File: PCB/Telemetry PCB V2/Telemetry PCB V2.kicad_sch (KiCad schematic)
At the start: 47 parts, among them IC1 E22-900M22S, J1 USB_C_Receptacle_USB2.0_16P, J2 Batt, J3 Serial Debug Header 1x4, J4 GPS, J5 Conn_01x04_Pin, SW1 SW_MEC_5E, SW2 SW_MEC_5E, U1 AP62200WU, U2 STM32F411CEUx, U3 MCP1700x-250xxTT, Y1 25MHZ 20pF, Y2 32.768k 12.5pF

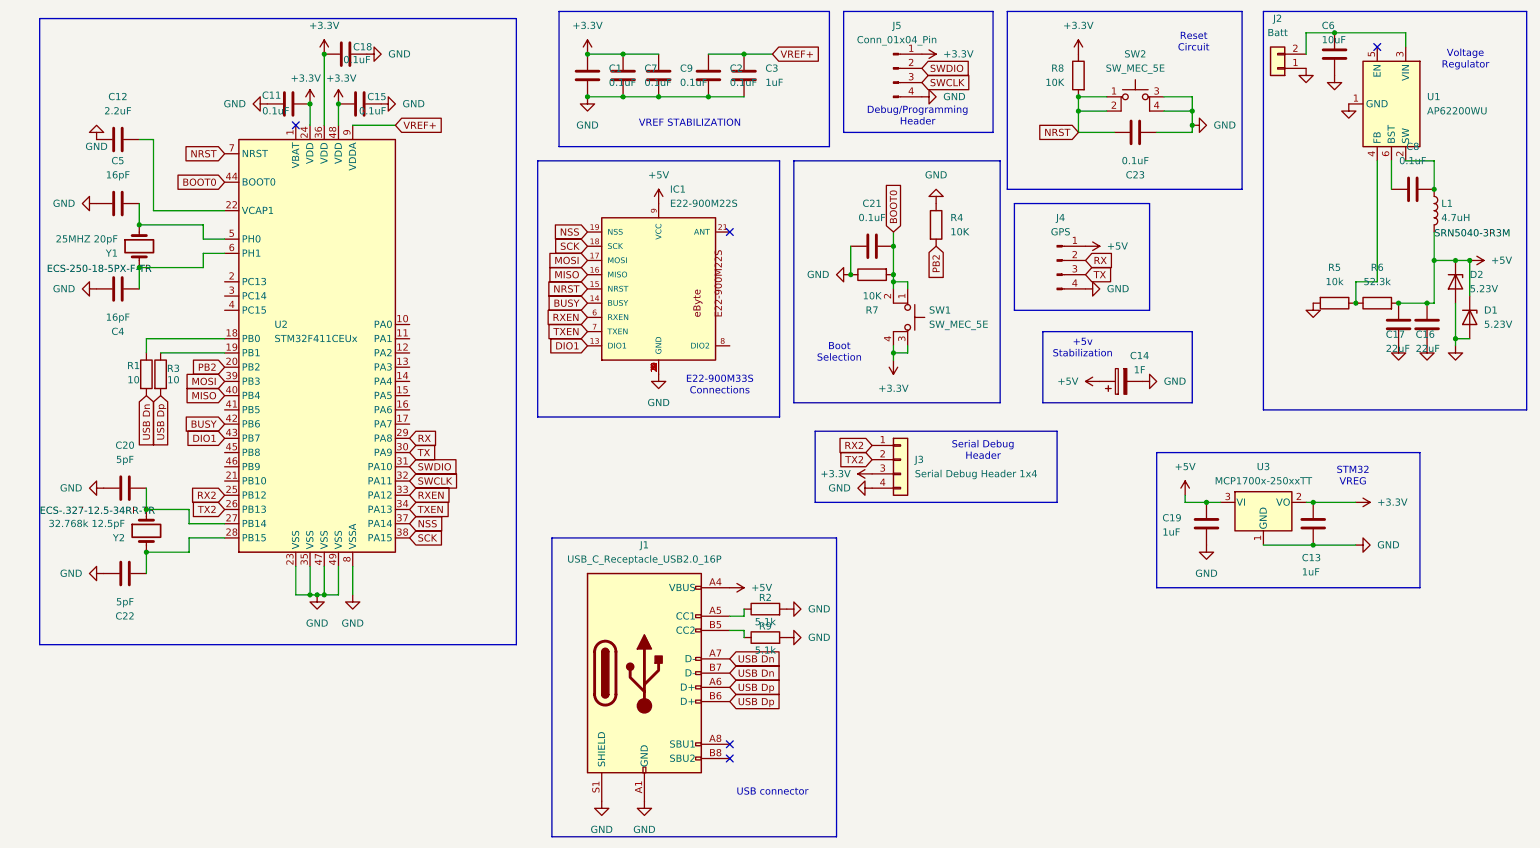
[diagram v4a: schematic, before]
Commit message: Corrected spi and uart connections
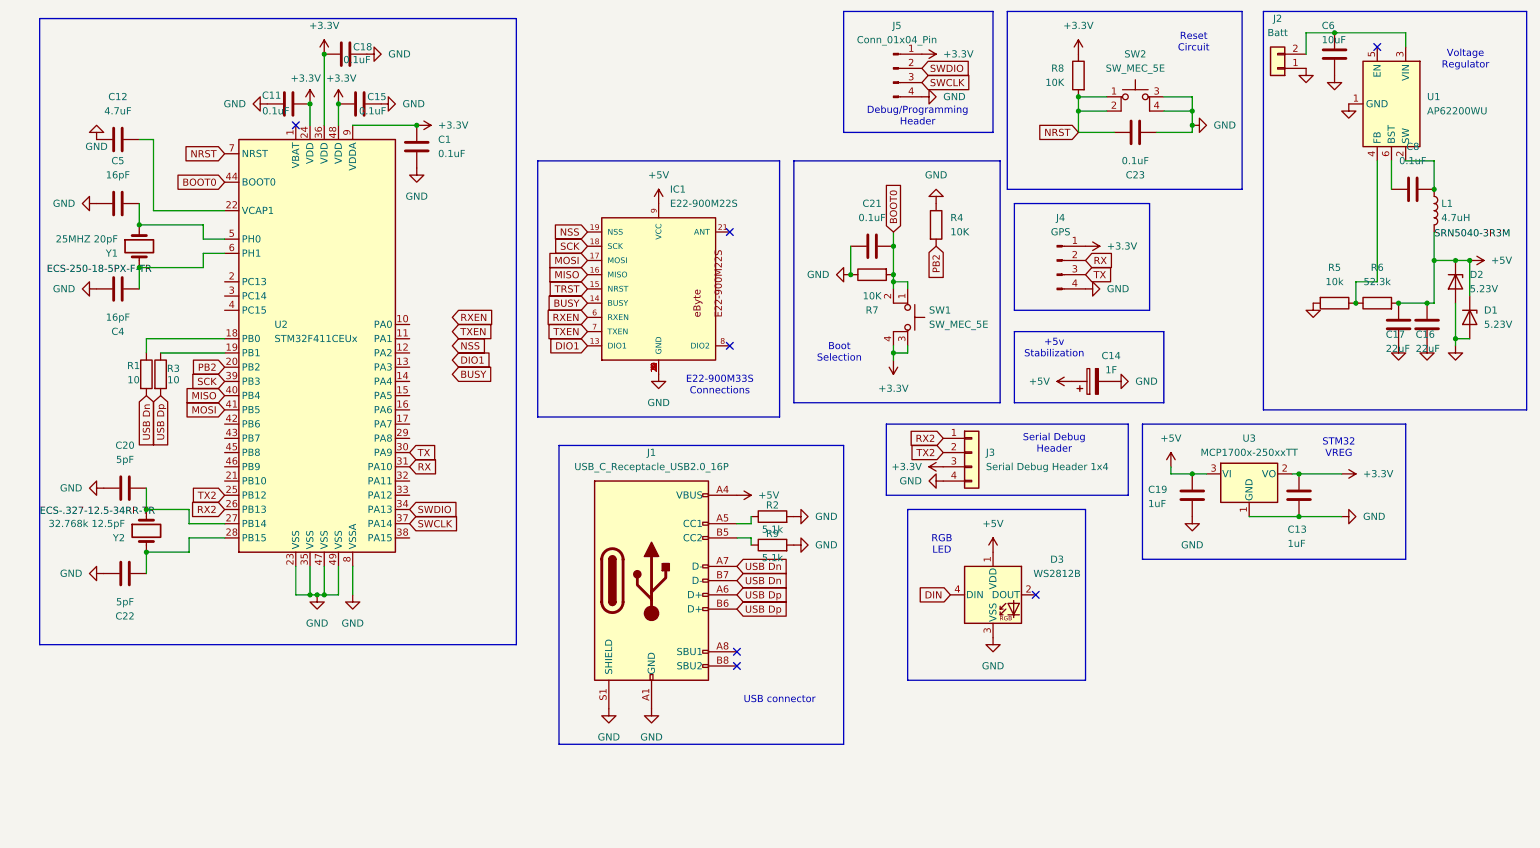
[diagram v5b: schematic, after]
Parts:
- removed C2, C7, C9: 0.1uF, Capacitor_SMD:C_1206_3216Metric_Pad1.33x1.80mm_HandSolder, symbol Device:C
- removed C3: 1uF, Capacitor_SMD:C_1206_3216Metric_Pad1.33x1.80mm_HandSolder, symbol Device:C
- added D3: WS2812B, LED_SMD:LED_WS2812B_PLCC4_5.0x5.0mm_P3.2mm, symbol LED:WS2812B
- C12: value 2.2uF -> 4.7uF
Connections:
- net VREF+ is gone; now on net +3.3V: U2.9 (VDDA)
- net +3.3V: now also C1.2, J4.1 (Pin_1); no longer C1.1
- net +5V: now also D3.1 (VDD); no longer J4.1 (Pin_1)
- net BUSY: no longer U2.42 (PB6)
- net DIO1: no longer U2.43 (PB7)
- net GND: now also C1.1, D3.3 (VSS); no longer C1.2
- net MOSI: now also U2.41 (PB5); no longer U2.39 (PB3)
- net NRST: no longer IC1.15 (NRST)
- net NSS: no longer U2.37 (PA14)
- net RX: now also U2.31 (PA10); no longer U2.29 (PA8)
- net RX2: now also U2.26 (PB13); no longer U2.25 (PB12)
- net RXEN: no longer U2.33 (PA12)
- net SCK: now also U2.39 (PB3); no longer U2.38 (PA15)
- net SWCLK: now also U2.37 (PA14); no longer U2.32 (PA11)
- net SWDIO: now also U2.34 (PA13); no longer U2.31 (PA10)
- net TX2: now also U2.25 (PB12); no longer U2.26 (PB13)
- net TXEN: no longer U2.34 (PA13)
- new net DIN: D3.4 (DIN)
- new net TRST: IC1.15 (NRST)
- no-connect marks 5 -> 7
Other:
- note added: "RGB LED"
- note removed: "VREF STABILIZATION"
- moved on the sheet: C13, C14, C19, J1, J3, R2, R9, U3

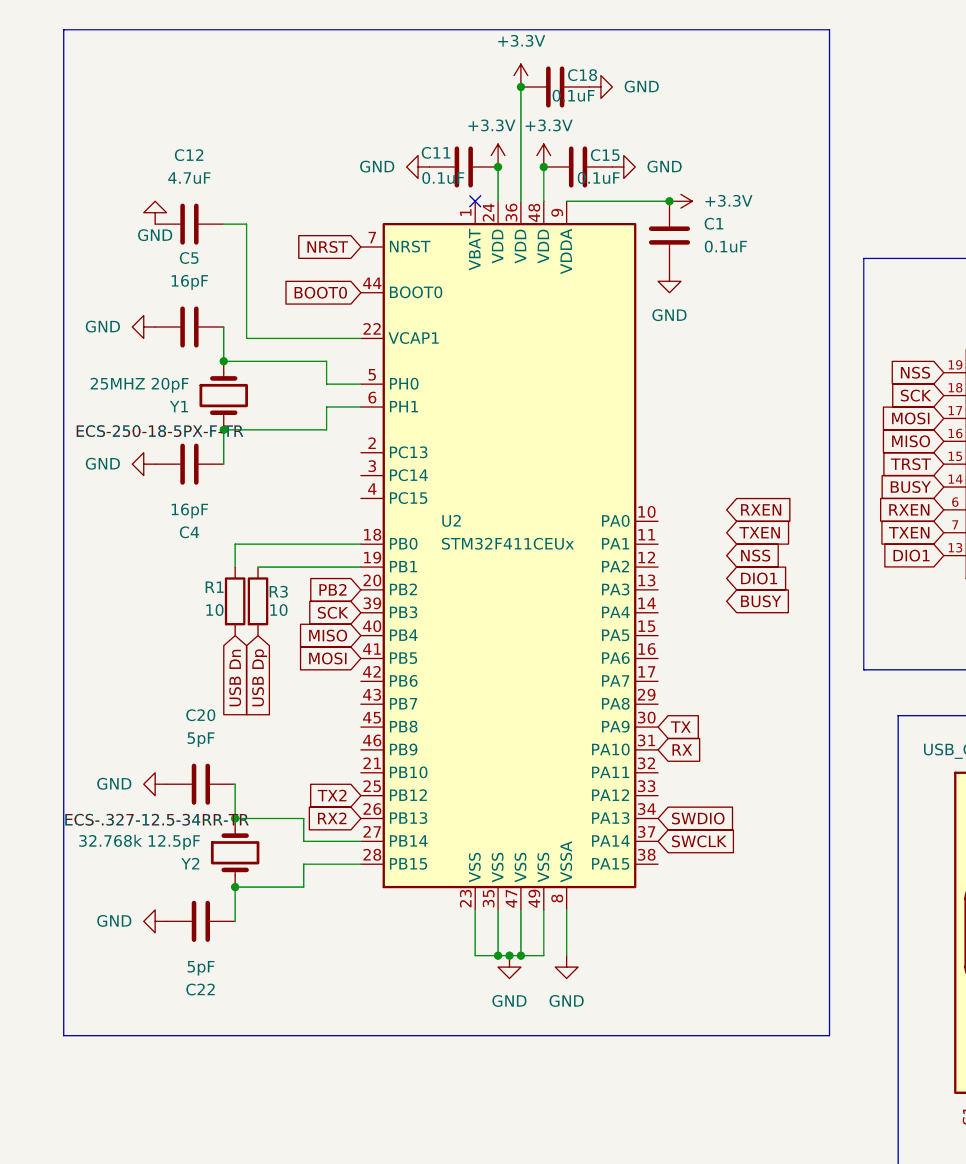
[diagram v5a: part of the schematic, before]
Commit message: Pins that were wrong are now right
Pins that were wrong are now right and also changed form 1206 capacitors to 0603 capacitors for the load capacitors on the low speed oscillator to reduce size for placement reasons.
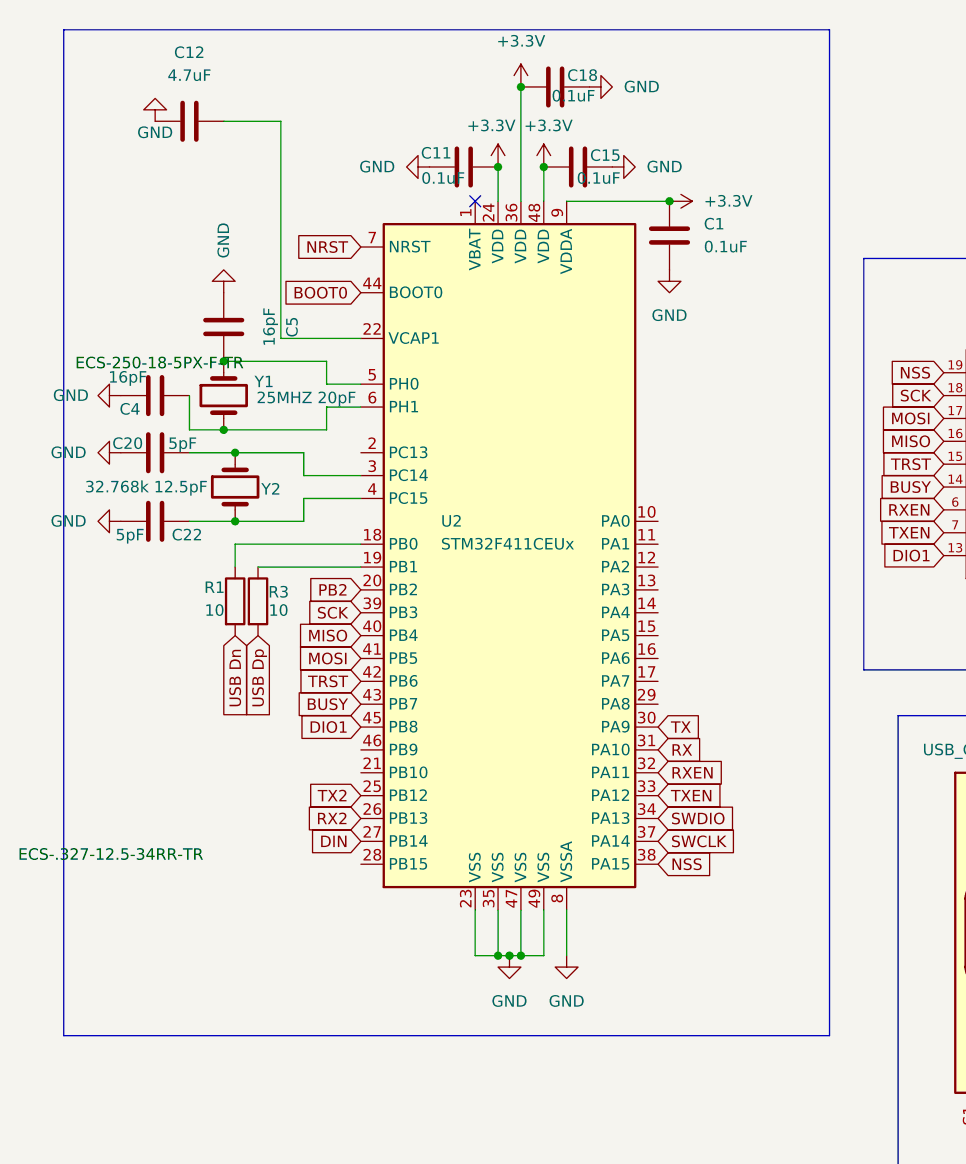
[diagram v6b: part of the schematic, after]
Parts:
- C20, C22: footprint Capacitor_SMD:C_1206_3216Metric_Pad1.33x1.80mm_HandSolder -> Capacitor_SMD:C_0603_1608Metric_Pad1.08x0.95mm_HandSolder
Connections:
- net BUSY: now also U2.43 (PB7)
- net DIN: now also U2.27 (PB14)
- net DIO1: now also U2.45 (PB8)
- net NSS: now also U2.38 (PA15)
- net RXEN: now also U2.32 (PA11)
- net TRST: now also U2.42 (PB6)
- net TXEN: now also U2.33 (PA12)
- net at C20.2, Y2.1: now also U2.3 (PC14); no longer U2.27 (PB14)
- net at C22.1, Y2.2: now also U2.4 (PC15); no longer U2.28 (PB15)
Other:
- moved on the sheet: C12, C20, C22, C4, C5, Y2

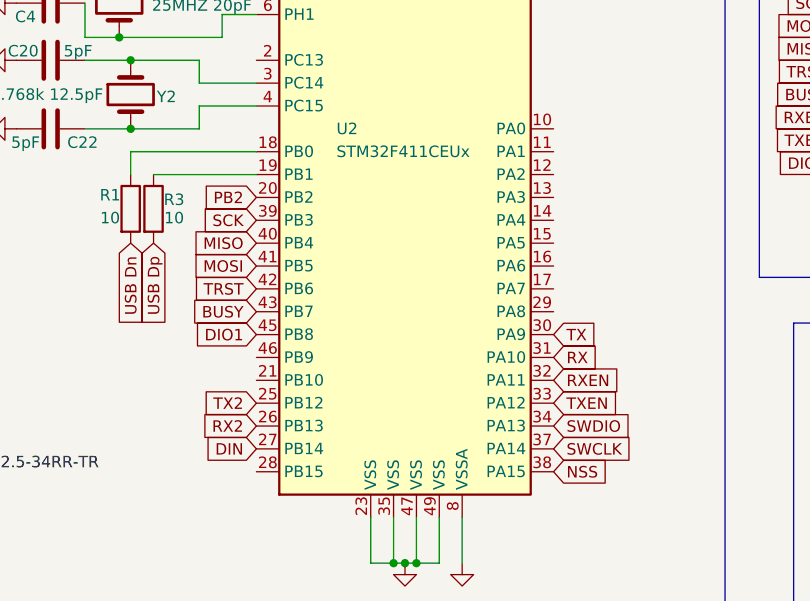
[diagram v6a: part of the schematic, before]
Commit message: changed many things
changed capacitor footprint, moved tx2 and rx2 to a uart pin. moved nrst switch moved j3 header
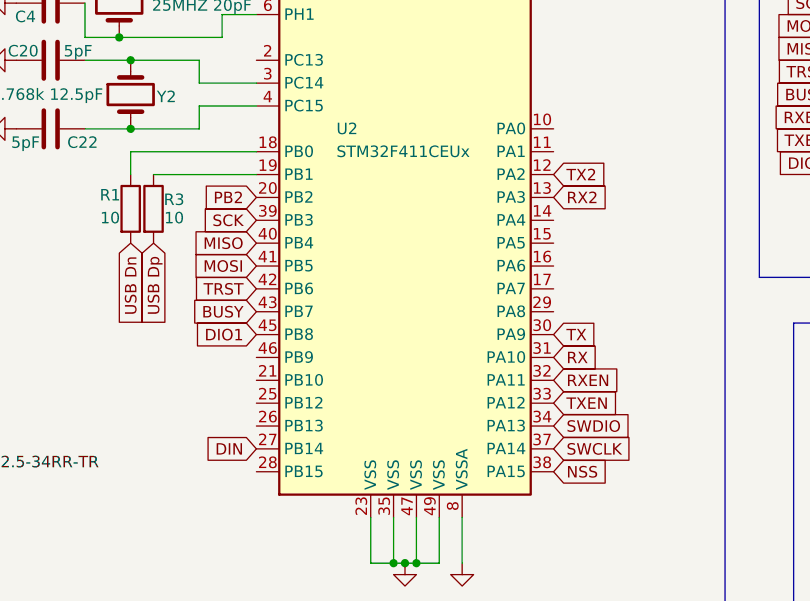
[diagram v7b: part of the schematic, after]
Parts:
- C14: footprint Capacitor_THT:C_Radial_D10.0mm_H20.0mm_P5.00mm -> PLZ5V1C_G3_H:C_Rect_L16.5mm_W8.7mm_P11.50mm_MKT
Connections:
- net RX2: now also U2.13 (PA3); no longer U2.26 (PB13)
- net TX2: now also U2.12 (PA2); no longer U2.25 (PB12)
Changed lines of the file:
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@@
 	(global_label "TX2"
 		(shape input)
-		(at 49.53 101.6 180)
+		(at 82.55 76.2 0)
 		(fields_autoplaced yes)
 		(effects
@@
 				(size 1.27 1.27)
 			)
-			(justify right)
+			(justify left)
 		)
 		(property "Intersheetrefs" "${INTERSHEET_REFS}"
-			(at 43.1582 101.6 0)
+			(at 88.9218 76.2 0)
 			(effects
 				(font
 					(size 1.27 1.27)
 				)
-				(justify right)
+				(justify left)
 				(hide yes)
 			)
@@
 	(global_label "RX2"
 		(shape input)
-		(at 49.53 104.14 180)
+		(at 82.55 78.74 0)
 		(fields_autoplaced yes)
 		(effects
@@
 				(size 1.27 1.27)
 			)
-			(justify right)
+			(justify left)
 		)
 		(property "Intersheetrefs" "${INTERSHEET_REFS}"
-			(at 42.8558 104.14 0)
+			(at 89.2242 78.74 0)
 			(effects
 				(font
 					(size 1.27 1.27)
 				)
-				(justify right)
+				(justify left)
 				(hide yes)
 			)
@@
 			)
 		)
-		(property "Footprint" "Capacitor_THT:C_Radial_D10.0mm_H20.0mm_P5.00mm"
+		(property "Footprint" "PLZ5V1C_G3_H:C_Rect_L16.5mm_W8.7mm_P11.50mm_MKT"
 			(at 208.28 80.3148 0)
 			(effects

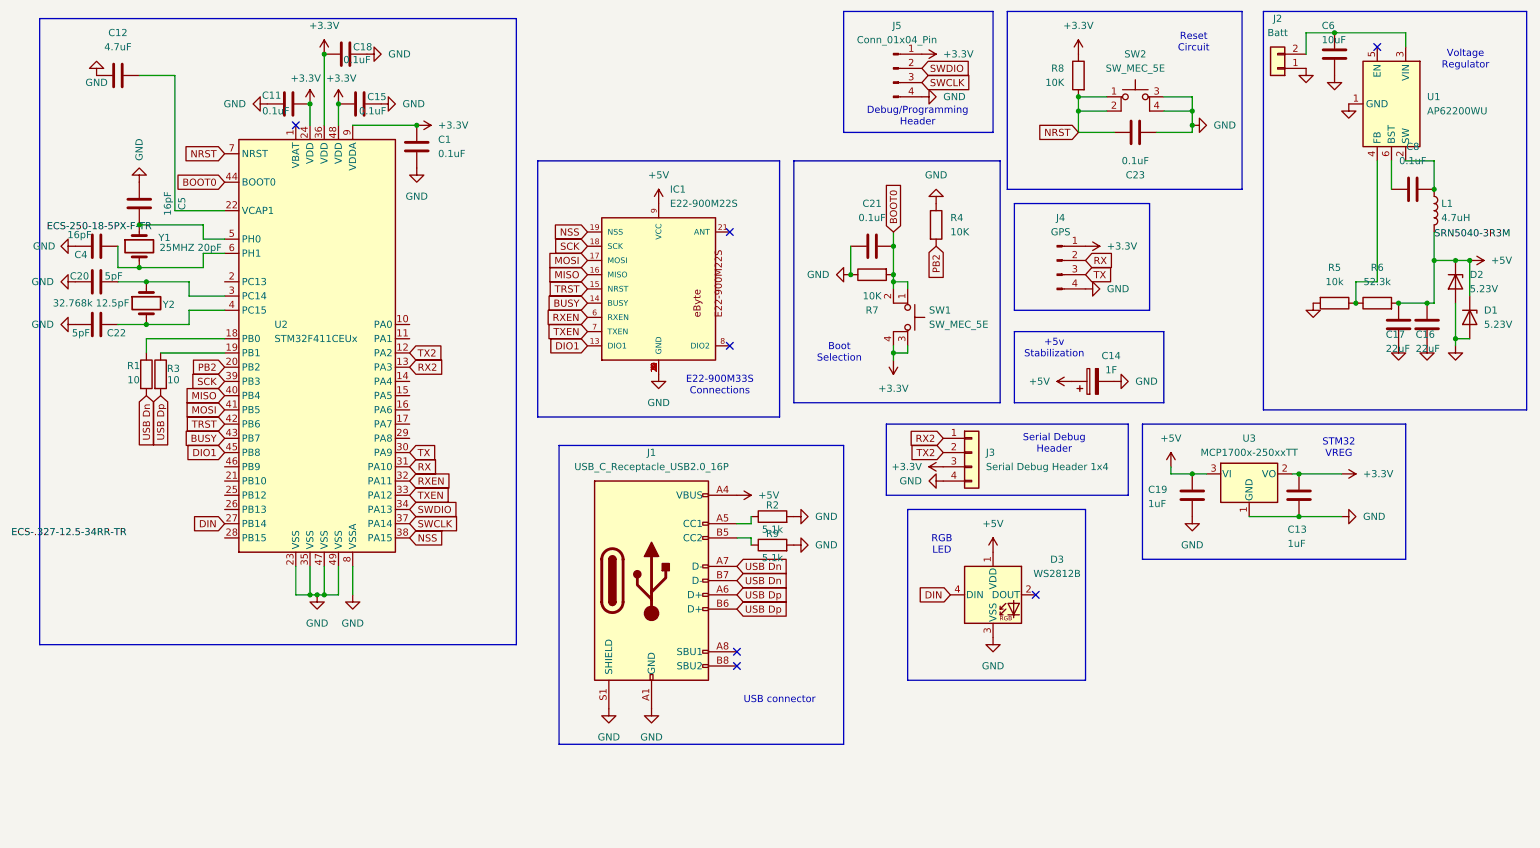
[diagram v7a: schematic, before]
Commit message: Revamped power, made usb better
Revamped the layout of the voltage regulator to match closer to the recommend layout form the data sheet.
Realized I didn't need vias for the usb lines so they are much nicer now
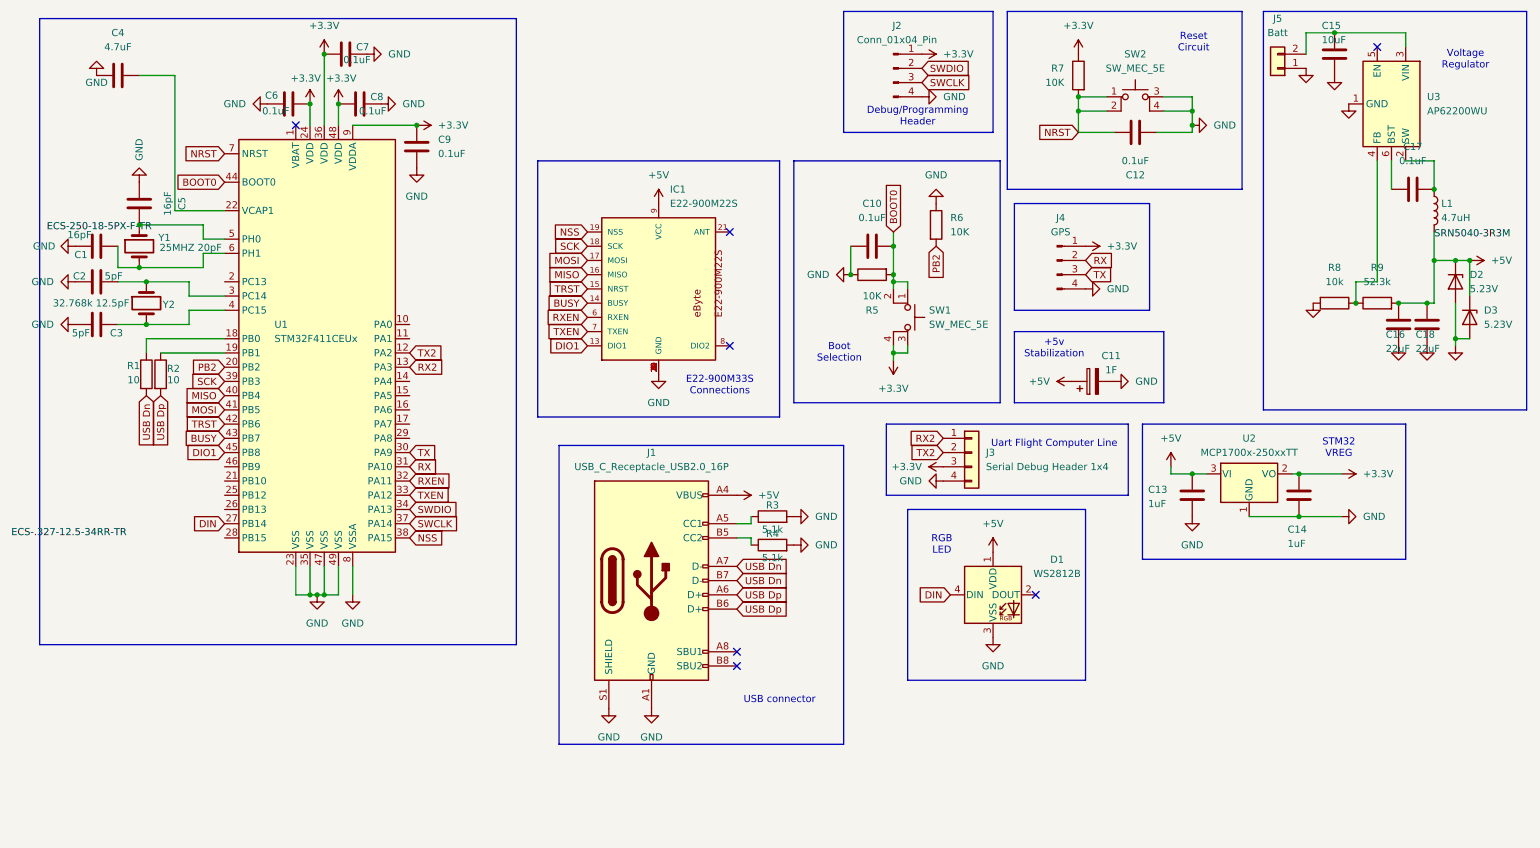
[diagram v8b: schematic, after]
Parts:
- C11: renamed from C14; footprint PLZ5V1C_G3_H:C_Rect_L16.5mm_W8.7mm_P11.50mm_MKT -> Custom Capacitor:C_Rect_L16.5mm_W8.7mm_P12.00mm_MKT
- renumbered C4 to C1, C21 to C10, C23 to C12, C19 to C13, C13 to C14, C6 to C15, C17 to C16, C8 to C17, C16 to C18, C20 to C2, C22 to C3, C12 to C4, C11 to C6, C18 to C7, C15 to C8, C1 to C9, D3 to D1, D1 to D3, J5 to J2, J2 to J5, R3 to R2, R2 to R3, R9 to R4, R7 to R5, R4 to R6, R8 to R7, R5 to R8, R6 to R9, U2 to U1, U3 to U2, U1 to U3
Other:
- note added: "Uart Flight Computer Line"
- note removed: "Serial Debug Header"
